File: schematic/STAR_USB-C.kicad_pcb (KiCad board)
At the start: 2 copper layers, 82.2 x 48.8 mm, 55 parts, among them J1 1017491, J2 1017491, J3 PD_DBG, J4 6120XX21621_61200621621, J5 Conn_01x02, J6 PD_I2C, J7 USB4216-03-A, U1 CAT24C512WI-GT3, U2 TPS25751DREFR, U3 TVS2200DRV

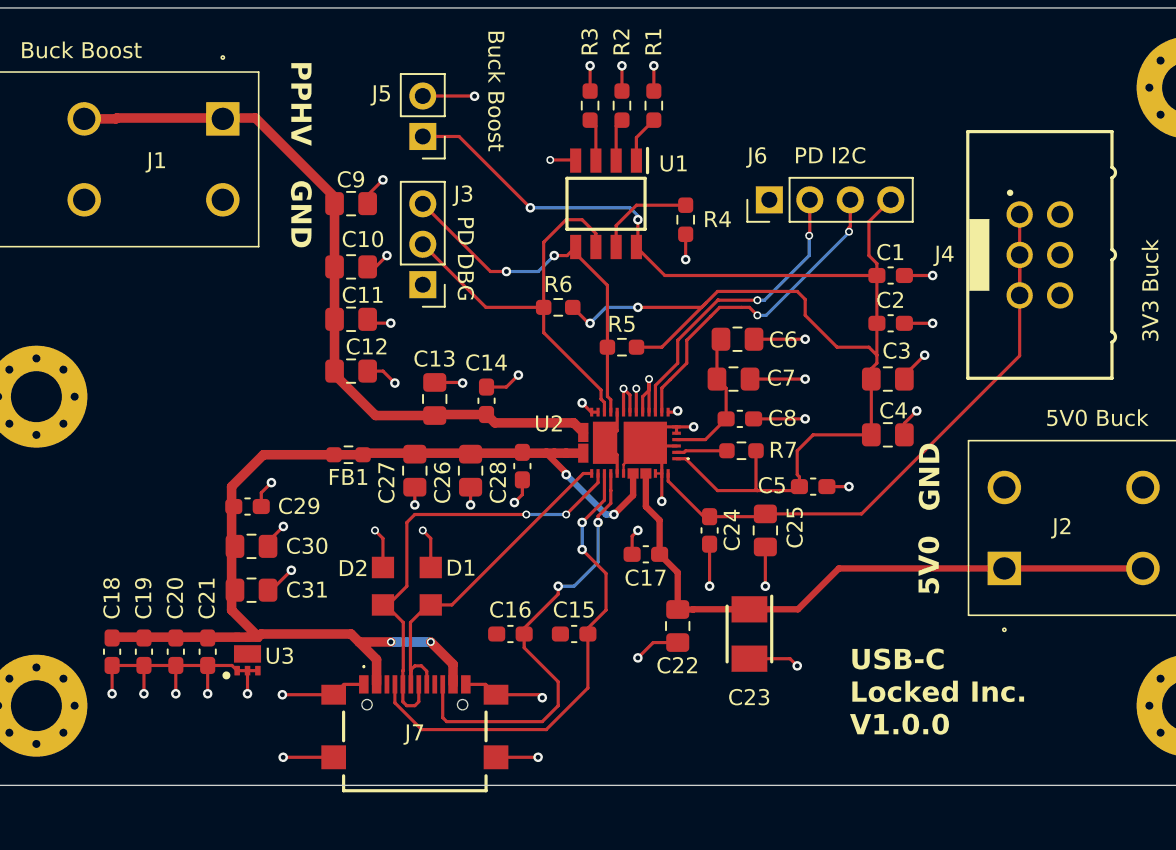
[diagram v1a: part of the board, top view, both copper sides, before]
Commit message: fixed usb-c
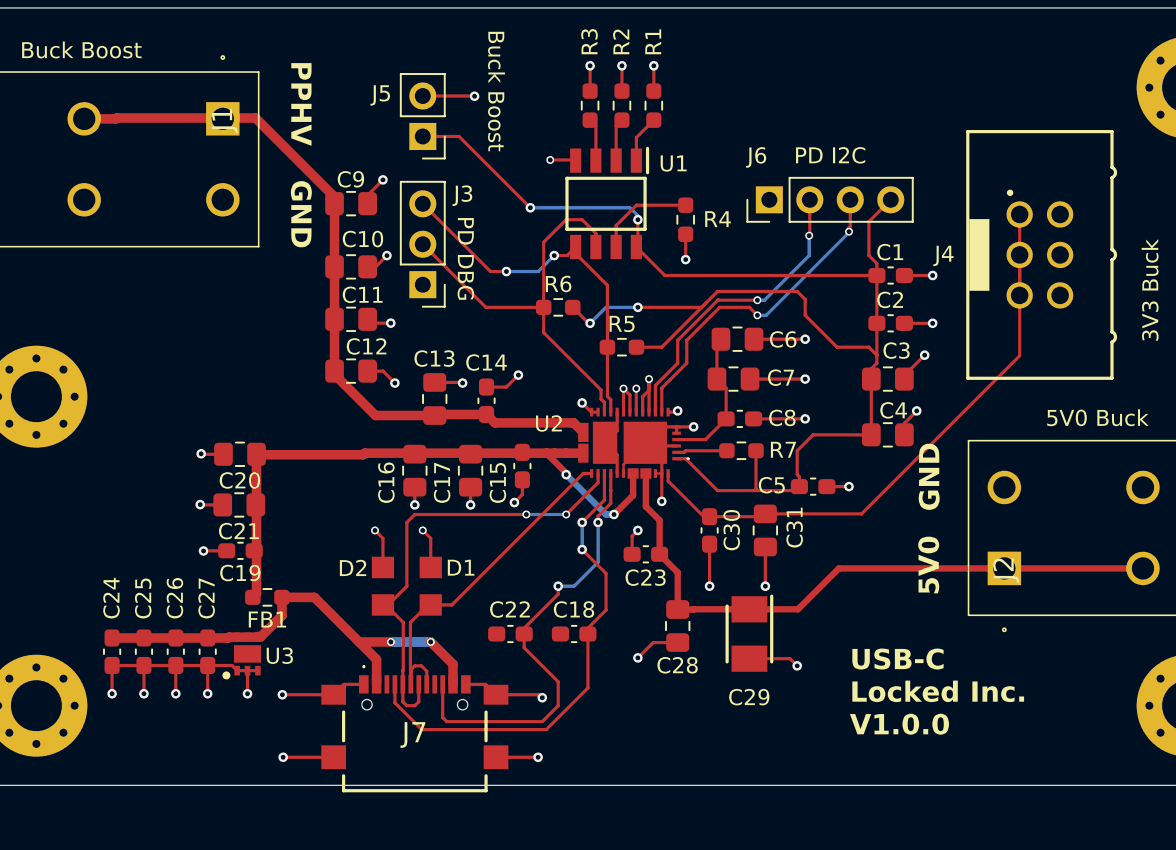
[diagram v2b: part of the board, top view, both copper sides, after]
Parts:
- removed the C29 at (95.0, 97.0)
- removed the C30 at (95.2, 99.5)
- removed the C31 at (95.2, 102.2)
- added C19: 100n, Capacitor_SMD:C_0603_1608Metric_Pad1.08x0.95mm_HandSolder, F.Cu at (94.6, 99.8)
- added C20: 4u7, Capacitor_SMD:C_0805_2012Metric_Pad1.18x1.45mm_HandSolder, F.Cu at (94.5, 93.7)
- added C21: 4u7, Capacitor_SMD:C_0805_2012Metric_Pad1.18x1.45mm_HandSolder, F.Cu at (94.5, 96.9)
- moved FB1 10.3 mm to (96.2, 102.7)
- renumbered C28 to C15, C27 to C16, C26 to C17, C15 to C18, C16 to C22, C17 to C23, C18 to C24, C19 to C25, C20 to C26, C21 to C27, C22 to C28, C23 to C29, C24 to C30, C25 to C31
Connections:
- C24 pad 2: /VBUS -> Net-(J7-VBUS_1)
- C25 pad 2: /VBUS -> Net-(J7-VBUS_1)
- C26 pad 2: /VBUS -> Net-(J7-VBUS_1)
- C27 pad 2: /VBUS -> Net-(J7-VBUS_1)
- FB1 pad 1: /VBUS -> Net-(J7-VBUS_1)
- J7 pad A4: /VBUS -> Net-(J7-VBUS_1)
- J7 pad B4: /VBUS -> Net-(J7-VBUS_1)
- U3 pad 4: /VBUS -> Net-(J7-VBUS_1)
- U3 pad 5: /VBUS -> Net-(J7-VBUS_1)
- U3 pad 6: /VBUS -> Net-(J7-VBUS_1)
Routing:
- net /VBUS: track 68.7 -> 38.2 mm, vias 4 -> 2
- net Net-(J7-VBUS_1): track 0.00 -> 29.3 mm, vias 0 -> 2
- net GND: track 123.4 -> 122.3 mm

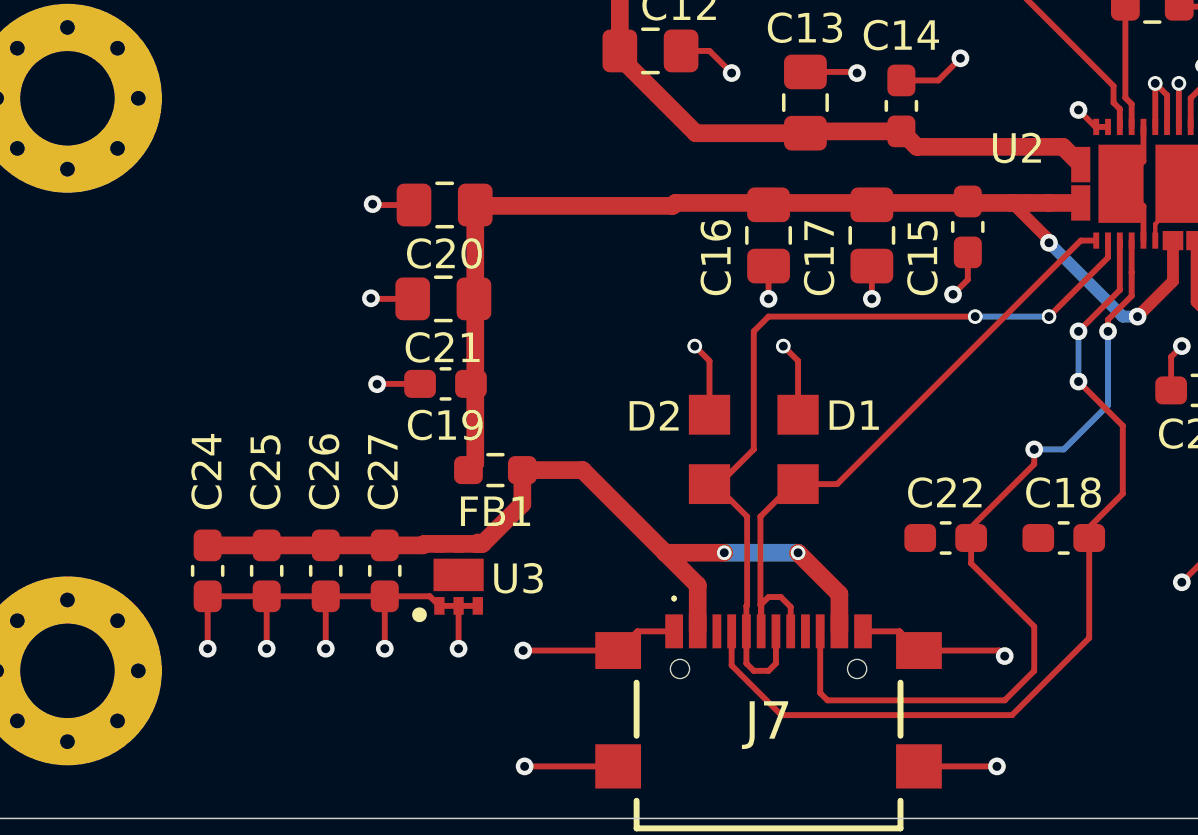
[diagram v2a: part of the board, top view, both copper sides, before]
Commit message: fixed usb-c
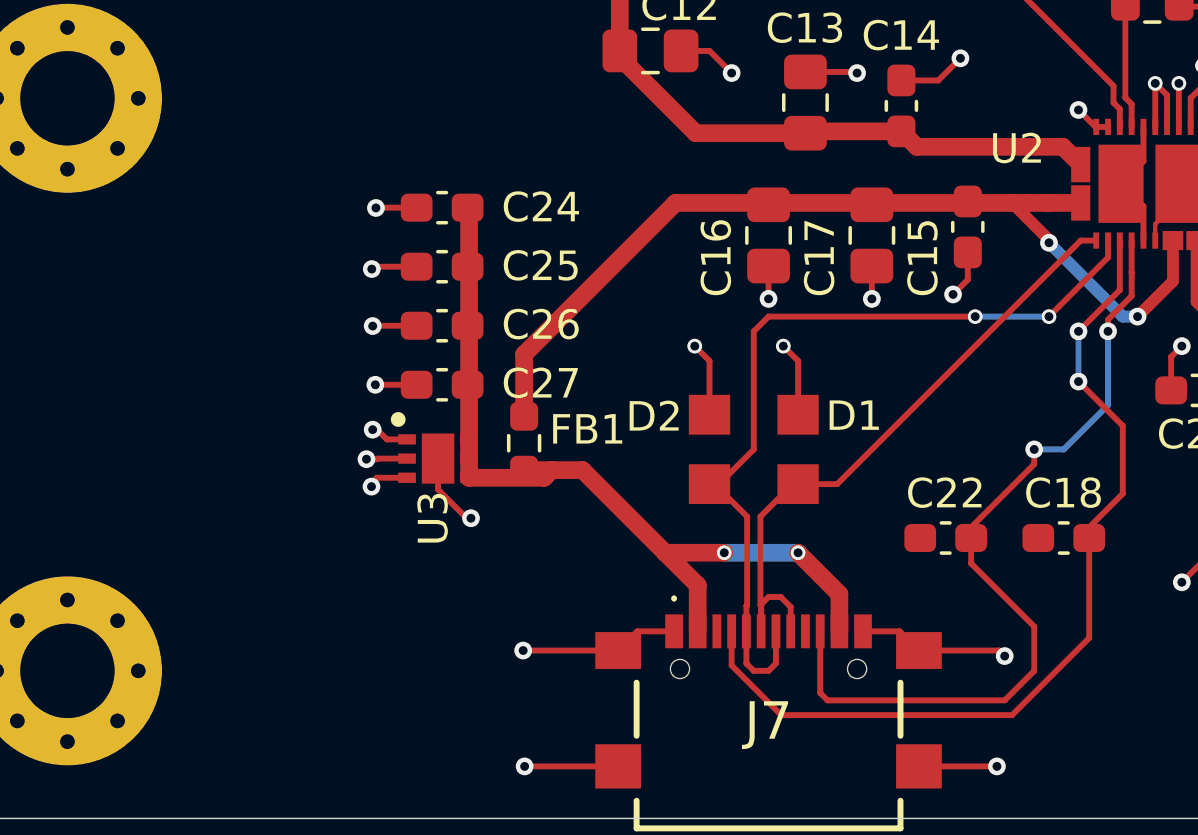
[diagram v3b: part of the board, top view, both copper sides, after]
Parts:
- removed C19: 100n, Capacitor_SMD:C_0603_1608Metric_Pad1.08x0.95mm_HandSolder
- removed C20, C21: 4u7, Capacitor_SMD:C_0805_2012Metric_Pad1.18x1.45mm_HandSolder
- moved C24 14.6 mm to (94.4, 93.8), turned to 0 degrees
- moved C25 11.9 mm to (94.4, 95.8), turned to 0 degrees
- moved C26 9.19 mm to (94.4, 97.8), turned to 0 degrees
- moved C27 6.60 mm to (94.4, 99.8), turned to 0 degrees
- moved U3 4.00 mm to (94.3, 102.3), turned to 0 degrees
- moved FB1 1.33 mm to (97.2, 101.8), turned to 90 degrees
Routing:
- net GND: track 122.3 -> 112.6 mm
- net /VBUS: track 38.2 -> 32.1 mm
